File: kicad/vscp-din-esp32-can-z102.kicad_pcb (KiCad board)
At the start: 2 copper layers, 47.8 x 84.8 mm, 39 parts, among them J1 Conn_01x05, J2 Conn_01x02, J3 Conn_01x06, J4 Conn_01x04, J5 Conn_01x04, J6 Conn_01x03, J7 Conn_01x05, J8 Conn_01x02, J9 Conn_01x02, U1 ESP32-C3-WROOM-02-N4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

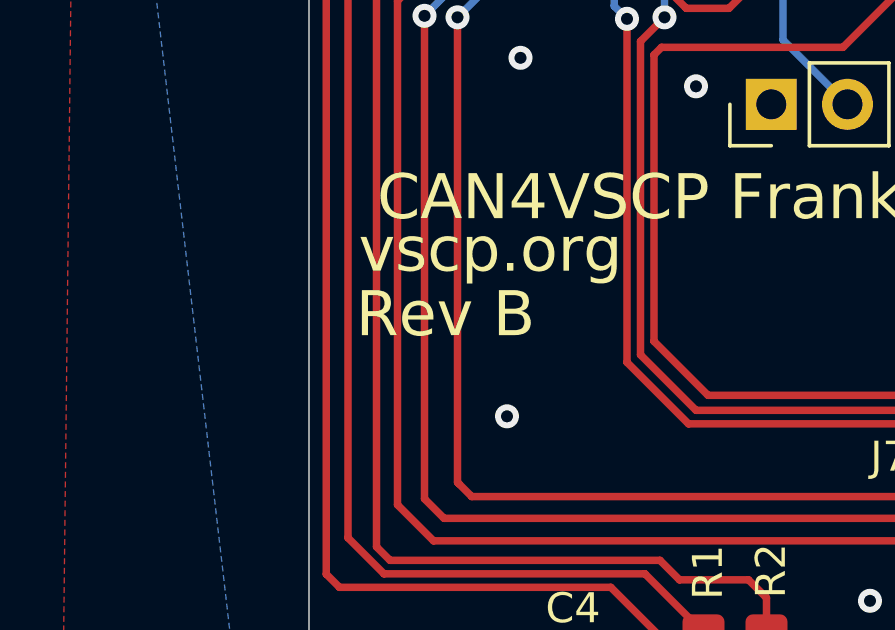
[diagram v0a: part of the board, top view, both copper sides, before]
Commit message: CAN <-> vscp-link working
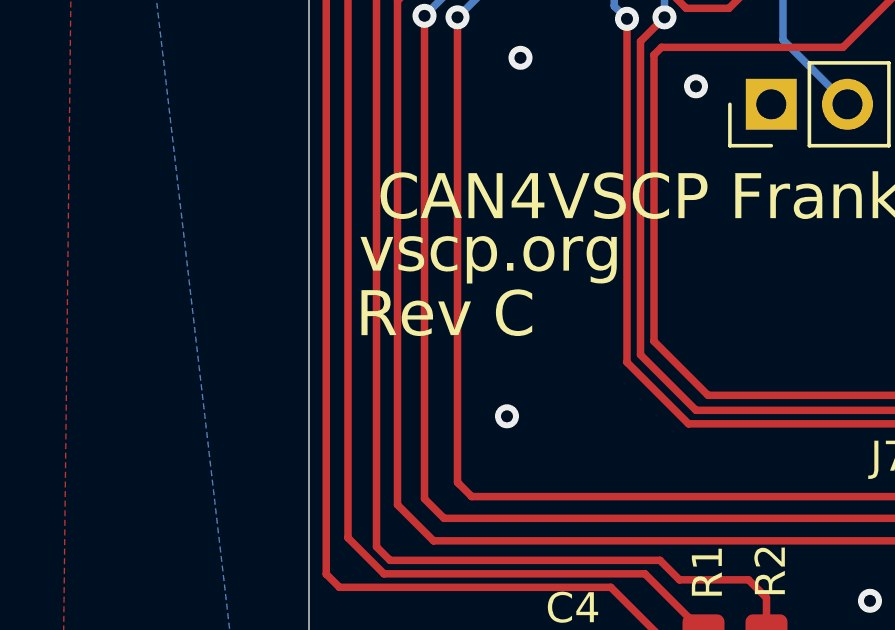
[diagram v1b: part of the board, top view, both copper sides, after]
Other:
- board text added: "Rev C"
- board text removed: "Rev B"
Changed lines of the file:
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@@
 		)
 	)
-	(gr_text "Rev B"
+	(gr_text "Rev C"
 		(at 124.25 131.6 0)
 		(layer "F.SilkS")
